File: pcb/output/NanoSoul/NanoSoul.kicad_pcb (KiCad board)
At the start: 2 copper layers, 96.6 x 92 mm, 62 parts, among them J1 JST_PH_B2B-PH-K_1x02_P2.00mm_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, J2 USB-C_SMD-TYPE-C-31-M-12_1, J3 PinSocket_1x20_P2.54mm_Vertic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, J4 PinSocket_1x20_P2.54mm_Vertic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, J5 PinHeader_1x06_P2.54mm_Vertic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, J6 PinHeader_1x06_P2.54mm_Vertic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, J7 PinHeader_1x06_P2.54mm_Vertic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, J8 JST_SH_BM04B-SRSS-TB_1x04-1MP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, Q1 SOT-23-6_L2.9-W1.6-P0.95-LS2.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, SW1 SW_SPST_CK_RS282G05A3, U1 SOT-23-6_L2.9-W1.6-P0.95-LS2.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, U2 ESOP-8_L4.9-W3.9-P1.27-LS6.0-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, U3 SOT-23-6_L2.9-W1.6-P0.95-LS2.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, U4 SSOP-24_L8.3-W5.6-P0.65-LS7.6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, U5 SSOP-24_L8.3-W5.6-P0.65-LS7.6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, U6 LGA-14_L3.0-W2.5-P0.50-BR

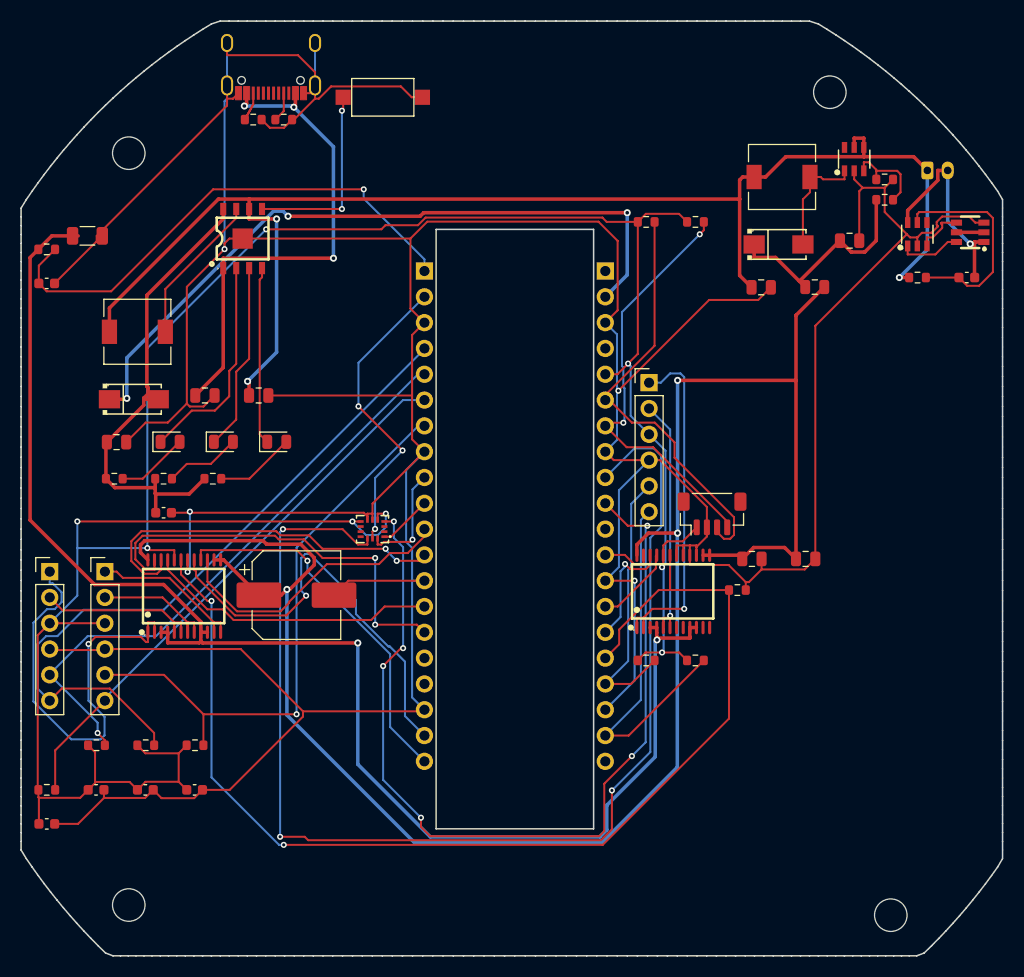
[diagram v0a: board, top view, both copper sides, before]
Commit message: pcb: 62×72mm 4层载板重设计 — 175/176 布通 DRC 0违规/0parity(零ignore)
从 50×50 目标逐步放宽到 62×72mm(用户逐次授权)达 headless 布线上界:
- 4层(F 信号 / In1 GND / In2 电源 / B 信号), 58 器件双面贴, 中槽 15.5×50,
  母排行距 17.8 冻结, 4 个 M3 角孔; 板框圆∩矩形 Ø88(R44) 四边切平
- Freerouting(best-of-N seed=2, 摆位质量主导需搜种子) 布净 175/176; route_fine 补 V3V3 小缝
- DRC: violations 0 · schematic-parity 0(62 检查全 error, 零 ignore) · 丝印干净
- 仅 USB_CC2(USB-C CC2 下拉 R6→J2.B5) 待手工收尾: B5 是 SMD 密脚+屏蔽柱围死、
  J2 在边缘,是 headless 栅格布线死角。route_cc2_manual.py 已证 0.2mm 穿脚缝可干净布
  (裸板 DRC=0),整合到全布板需 KiCad GUI push-and-shove(~2 分钟)。

血泪结论(见记忆 project_nanosoul_headless_routing_limit): 此设计 headless 0/0 需放大;
route_fine 布长跨槽网必擦铜、只 Freerouting 能干净布; 给够面积(≥76×86)可全自布但板明显变大。

新脚本: route_fine(局部细栅格迷宫补漏,via作走线障碍/端点禁孔逼F.Cu逃逸) /
route_cc2_manual(USB-C CC2 逃逸,自校验净空) / reroute_a_keepall(增量布线) /
drop_leds(外科式去件保 ref) / route2_4l / connect_exact / reroute_a_gnd
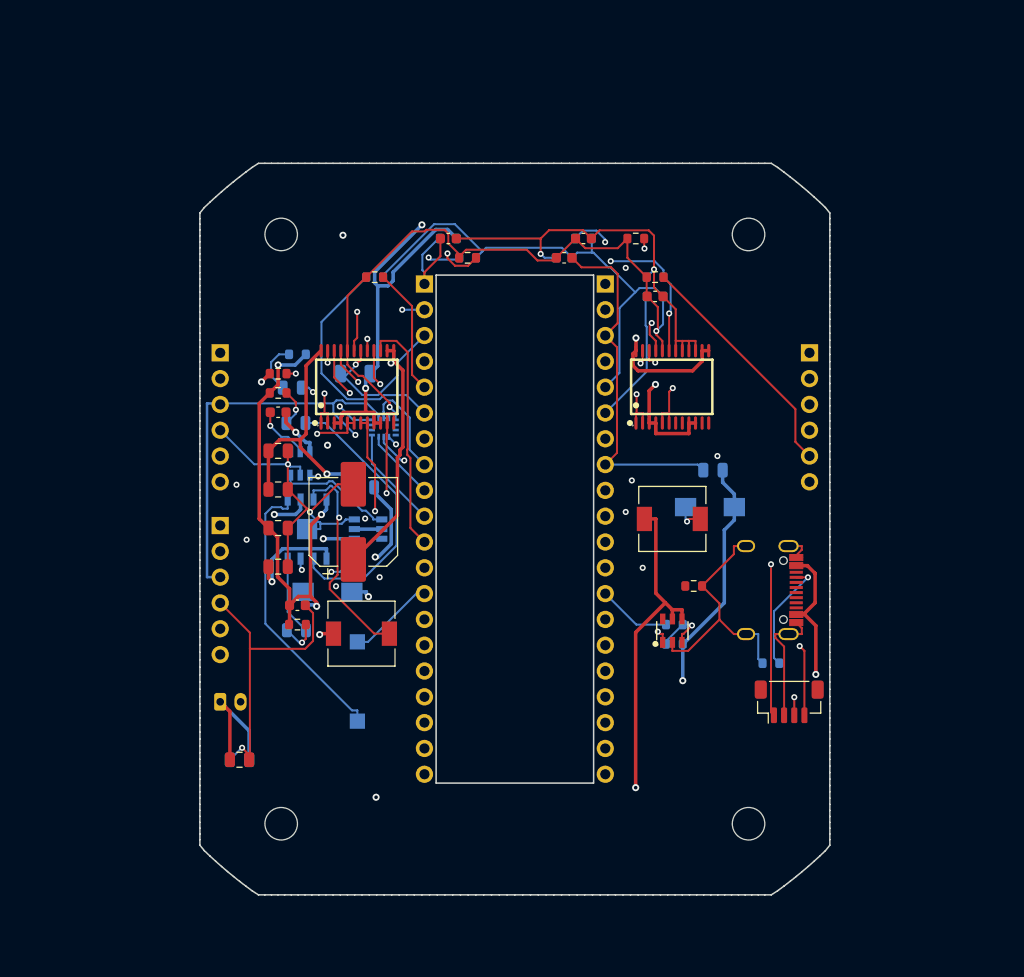
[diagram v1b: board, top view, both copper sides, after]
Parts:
- C14, C2, C7, D1, D2, D3, D4, D5, F1, J5, J6, J7, Q1, R10, R11, R14, R15, R18, R19, R3, R5, R7, R8, R9, SW1, U1, U2, U6: moved to B.Cu
- moved J1 87.1 mm to (121.0, 117.0)
- moved C15 78.2 mm to (156.8, 71.4)
- moved C10 73.4 mm to (163.8, 77.1)
- moved R5 71.8 mm to (175.2, 113.2), turned to 180 degrees
- moved J2 71.2 mm to (175.2, 106.0), turned to -90 degrees
- moved C6 69.3 mm to (122.9, 122.7)
- moved C1 69.1 mm to (126.7, 88.5)
- moved C12 66.6 mm to (154.8, 73.3)
- moved Q1 66.1 mm to (135.6, 100.0), turned to 180 degrees
- moved U1 64.8 mm to (128.9, 93.5), turned to 180 degrees
- moved C14 63.8 mm to (154.8, 73.3), turned to 180 degrees
- moved R1 63.6 mm to (126.7, 84.7)
- moved R6 63.1 mm to (167.6, 105.6)
- moved R15 59.9 mm to (136.2, 75.2), turned to 180 degrees
- moved SW1 57.6 mm to (134.5, 115.0), turned to 90 degrees
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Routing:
- net GND: track 508.0 -> 393.8 mm, vias 5 -> 6
- net VMOT: track 21.7 -> 93.0 mm, vias 0 -> 3
- net VMOT_F: track 185.4 -> 116.8 mm, vias 3 -> 4
- net CHG_IN: track 49.7 -> 116.7 mm, vias 3 -> 2
- net MOT_RTN: track 142.8 -> 87.5 mm, vias 2 -> 3
- net IMU_CS: track 118.9 -> 71.5 mm, vias 3 -> 2
- net MOT_ISENSE: track 51.0 -> 10.5 mm, vias 1 -> 0
- net V3V3: track 248.6 -> 210.0 mm, vias 8 -> 4
- net M2_ENC_B: track 36.6 -> 74.2 mm, vias 0 -> 1
- net M2_ENC_A: track 27.1 -> 60.9 mm, vias 0 -> 1
- net MOTOR_STBY: track 113.6 -> 84.1 mm, vias 2 -> 3
- net M0_ENC_B: track 70.0 -> 42.5 mm, vias 0 -> 1
- net M0_OUT_A: track 43.3 -> 16.4 mm
- net M2_IN1: track 7.86 -> 34.2 mm, vias 0 -> 1
- net M2_IN2: track 11.3 -> 32.1 mm
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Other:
- board size 96.6 x 92 mm -> 62 x 72 mm
- copper layers 2 -> 4
